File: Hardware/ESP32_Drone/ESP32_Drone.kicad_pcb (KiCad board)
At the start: 2 copper layers, 50 x 50 mm, 75 parts, among them J1 USB_C_Receptacle_USB2.0_16P, J2 Conn_01x02_Socket, J3 Conn_01x02_Socket, J4 Conn_01x02_Socket, J5 Conn_01x02_Socket, J6 Conn_01x02_Socket, Q1 AO3401A, Q2 SS8050, Q3 SS8050, Q4 AO3400A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

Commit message: JCSC field added.
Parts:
- R7: value 2k -> 1k
- R8: value 22.1k -> 22k
- R9: value 47.5k -> 47k

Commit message: PCB layout v1.0
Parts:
- R18, R19: value 1.3k -> 1k
- moved SW1 46.4 mm to (265.5, 114.5), turned to 90 degrees
- moved R6 31.9 mm to (259.5, 110.5), turned to 90 degrees
- moved C10 17.0 mm to (256.5, 141.9), turned to -90 degrees
- moved R21 12.4 mm to (251.1, 123.0)
- moved R11 12.0 mm to (231.0, 118.0)
- moved R10 11.9 mm to (232.5, 118.0)
- moved C11 11.7 mm to (254.0, 142.1), turned to -90 degrees
- moved R28 10.8 mm to (258.0, 138.5), turned to -90 degrees
- moved J3 10.2 mm to (265.9, 137.8), turned to 90 degrees
- moved C4 9.35 mm to (236.0, 107.0)
- moved R23 8.92 mm to (225.5, 140.5)
- moved C16 8.55 mm to (226.0, 103.0)
- moved R22 8.50 mm to (225.5, 142.5)
- moved R7 8.14 mm to (226.5, 109.0), turned to 0 degrees
- moved Q4 7.68 mm to (261.8, 129.5), turned to 0 degrees
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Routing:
- net +BATT: track 0.00 -> 165.5 mm, vias 0 -> 6
- net +3.3V: track 0.00 -> 100.4 mm, vias 0 -> 6
- net VBUS: track 0.00 -> 76.3 mm, vias 0 -> 2
- net GND: track 0.00 -> 70.4 mm, vias 0 -> 25
- net /ESP32_EN: track 0.00 -> 48.7 mm, vias 0 -> 2
- net /VIN: track 0.00 -> 42.0 mm
- net /PWM4: track 0.00 -> 38.6 mm, vias 0 -> 2
- net /PWM2: track 0.00 -> 37.5 mm, vias 0 -> 2
- net /PWM3: track 0.00 -> 35.3 mm
- net /SCL: track 0.00 -> 30.8 mm, vias 0 -> 2
- net /SDA: track 0.00 -> 29.2 mm, vias 0 -> 4
- net /ESP32_TX: track 0.00 -> 25.8 mm, vias 0 -> 2
- net /DTR: track 0.00 -> 25.0 mm, vias 0 -> 2
- net /MPU_INT: track 0.00 -> 25.0 mm, vias 0 -> 2
- net /ESP32_RX: track 0.00 -> 22.6 mm, vias 0 -> 2
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- added copper zone on F.Cu, net +3.3V
- added copper zone on B.Cu, net GND
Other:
- board text added: "Drone ESP32"
- board text added: "by Milos Nedeljkovic"

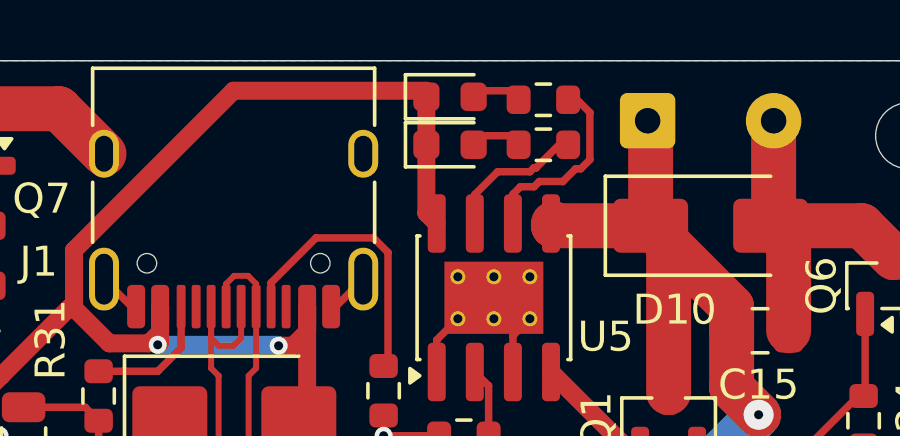
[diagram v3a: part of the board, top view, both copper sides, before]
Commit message: Fixed charger LEDs.
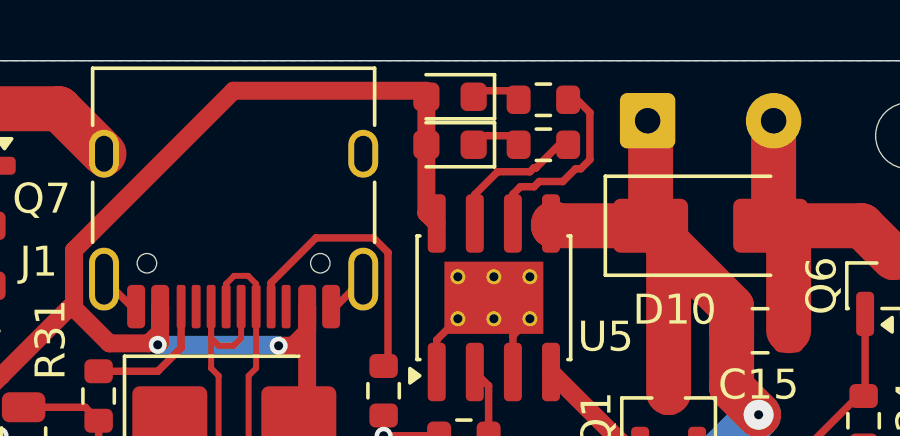
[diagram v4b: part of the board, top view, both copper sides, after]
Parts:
- turned D2 to 180 degrees
- turned D3 to 180 degrees
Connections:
- D2 pad 1: VBUS -> Net-(D2-K)
- D2 pad 2: Net-(D2-A) -> VBUS
- D3 pad 1: VBUS -> Net-(D3-K)
- D3 pad 2: Net-(D3-A) -> VBUS
- R18 pad 1: Net-(D2-A) -> Net-(D2-K)
- R19 pad 2: Net-(D3-A) -> Net-(D3-K)
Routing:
- net Net-(D3-K): track 0.00 -> 1.50 mm
- net Net-(D3-A): track 1.50 -> 0.00 mm
- net Net-(D2-K): track 0.00 -> 1.50 mm
- net Net-(D2-A): track 1.50 -> 0.00 mm
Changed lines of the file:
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@@
 			(layers "F.Cu" "F.Mask" "F.Paste")
 			(roundrect_rratio 0.25)
-			(net "Net-(D3-A)")
+			(net "Net-(D3-K)")
 			(pintype "passive")
 		)
@@
 	(footprint "LED_SMD:LED_0603_1608Metric"
 		(layer "F.Cu")
-		(at 250.2125 95.7)
+		(at 250.2125 95.7 180)
 		(descr "LED SMD 0603 (1608 Metric), square (rectangular) end terminal, IPC-7351 nominal, (Body size source: http://www.tortai-tech.com/upload/download/2011102023233369053.pdf)")
 		(tags "LED")
@@
 		)
 		(property "Sim.Pins" "1=K 2=A"
-			(at 0 0 0)
+			(at 0 0 180)
 			(unlocked yes)
 			(layer "F.Fab")
@@
 		)
 		(property "LCSC" "C2290"
-			(at 0 0 0)
+			(at 0 0 180)
 			(unlocked yes)
 			(layer "F.Fab")
@@
 		(duplicate_pad_numbers_are_jumpers no)
 		(fp_line
-			(start -1.485 -0.735)
-			(end -1.485 0.735)
+			(start 0.8 -0.735)
+			(end -1.485 -0.735)
 			(stroke
 				(width 0.12)
@@
 		)
 		(fp_line
-			(start 0.8 -0.735)
-			(end -1.485 -0.735)
+			(start -1.485 -0.735)
+			(end -1.485 0.735)
 			(stroke
 				(width 0.12)
@@
 		)
 		(fp_line
-			(start -0.8 -0.1)
-			(end -0.8 0.4)
+			(start 0.8 0.4)
+			(end 0.8 -0.4)
 			(stroke
 				(width 0.1)
@@
 		)
 		(fp_line
-			(start -0.8 0.4)
-			(end 0.8 0.4)
+			(start 0.8 -0.4)
+			(end -0.5 -0.4)
 			(stroke
 				(width 0.1)
@@
 		)
 		(fp_line
-			(start 0.8 -0.4)
-			(end -0.5 -0.4)
+			(start -0.8 0.4)
+			(end 0.8 0.4)
 			(stroke
 				(width 0.1)
@@
 		)
 		(fp_line
-			(start 0.8 0.4)
-			(end 0.8 -0.4)
+			(start -0.8 -0.1)
+			(end -0.8 0.4)
 			(stroke
 				(width 0.1)
@@
 		)
 		(pad "1" smd roundrect
-			(at -0.7875 0)
+			(at -0.7875 0 180)
 			(size 0.875 0.95)
 			(layers "F.Cu" "F.Mask" "F.Paste")
 			(roundrect_rratio 0.25)
-			(net "VBUS")
+			(net "Net-(D3-K)")
 			(pinfunction "K_1")
 			(pintype "passive")
 		)
 		(pad "2" smd roundrect
-			(at 0.7875 0)
+			(at 0.7875 0 180)
 			(size 0.875 0.95)
 			(layers "F.Cu" "F.Mask" "F.Paste")
 			(roundrect_rratio 0.25)
-			(net "Net-(D3-A)")
+			(net "VBUS")
 			(pinfunction "A_2")
 			(pintype "passive")
@@
 	(footprint "LED_SMD:LED_0603_1608Metric"
 		(layer "F.Cu")
-		(at 250.2125 97.3)
+		(at 250.2125 97.3 180)
 		(descr "LED SMD 0603 (1608 Metric), square (rectangular) end terminal, IPC-7351 nominal, (Body size source: http://www.tortai-tech.com/upload/download/2011102023233369053.pdf)")
 		(tags "LED")
@@
 		)
 		(property "Sim.Pins" "1=K 2=A"
-			(at 0 0 0)
+			(at 0 0 180)
 			(unlocked yes)
 			(layer "F.Fab")
@@
 		)
 		(property "LCSC" "C2286"
-			(at 0 0 0)
+			(at 0 0 180)
 			(unlocked yes)
 			(layer "F.Fab")
@@
 		(duplicate_pad_numbers_are_jumpers no)
 		(fp_line
-			(start -1.485 -0.735)
-			(end -1.485 0.735)
+			(start 0.8 -0.735)
+			(end -1.485 -0.735)
 			(stroke
 				(width 0.12)
@@
 		)
 		(fp_line
-			(start 0.8 -0.735)
-			(end -1.485 -0.735)
+			(start -1.485 -0.735)
+			(end -1.485 0.735)
 			(stroke
 				(width 0.12)
@@
 		)
 		(fp_line
-			(start -0.8 -0.1)
-			(end -0.8 0.4)
+			(start 0.8 0.4)
+			(end 0.8 -0.4)
 			(stroke
 				(width 0.1)
@@
 		)
 		(fp_line
-			(start -0.8 0.4)
-			(end 0.8 0.4)
+			(start 0.8 -0.4)
+			(end -0.5 -0.4)
 			(stroke
 				(width 0.1)
@@
 		)
 		(fp_line
-			(start 0.8 -0.4)
-			(end -0.5 -0.4)
+			(start -0.8 0.4)
+			(end 0.8 0.4)
 			(stroke
 				(width 0.1)
@@
 		)
 		(fp_line
-			(start 0.8 0.4)
-			(end 0.8 -0.4)
+			(start -0.8 -0.1)
+			(end -0.8 0.4)
 			(stroke
 				(width 0.1)
@@
 		)
 		(pad "1" smd roundrect
-			(at -0.7875 0)
+			(at -0.7875 0 180)
 			(size 0.875 0.95)
 			(layers "F.Cu" "F.Mask" "F.Paste")
 			(roundrect_rratio 0.25)
-			(net "VBUS")
+			(net "Net-(D2-K)")
 			(pinfunction "K_1")
 			(pintype "passive")
 		)
 		(pad "2" smd roundrect
-			(at 0.7875 0)
+			(at 0.7875 0 180)
 			(size 0.875 0.95)
 			(layers "F.Cu" "F.Mask" "F.Paste")
 			(roundrect_rratio 0.25)
-			(net "Net-(D2-A)")
+			(net "VBUS")
 			(pinfunction "A_2")
 			(pintype "passive")
@@
 			(layers "F.Cu" "F.Mask" "F.Paste")
 			(roundrect_rratio 0.25)
-			(net "Net-(D2-A)")
+			(net "Net-(D2-K)")
 			(pintype "passive")
 		)
@@
 	)
 	(segment
-		(start 251 95.5)
-		(end 252.5 95.5)
-		(width 0.25)
-		(layer "F.Cu")
-		(net "Net-(D3-A)")
-	)
-	(segment
 		(start 235 102)
 		(end 235 98)
@@
 	)
 	(segment
-		(start 251 97)
-		(end 252.5 97)
-		(width 0.25)
-		(layer "F.Cu")
-		(net "Net-(D2-A)")
-	)
-	(segment
 		(start 253.45 111.3625)
 		(end 253.6625 111.3625)
@@
 		(net "Net-(J1-CC1)")
 	)
+	(segment
+		(start 251 97)
+		(end 252.5 97)
+		(width 0.25)
+		(layer "F.Cu")
+		(net "Net-(D2-K)")
+	)
+	(segment
+		(start 251 95.5)
+		(end 252.5 95.5)
+		(width 0.25)
+		(layer "F.Cu")
+		(net "Net-(D3-K)")
+	)
 	(zone
